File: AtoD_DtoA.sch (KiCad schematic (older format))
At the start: 21 parts

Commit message: redo annotations
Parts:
- gave numbers to parts that had none: 21

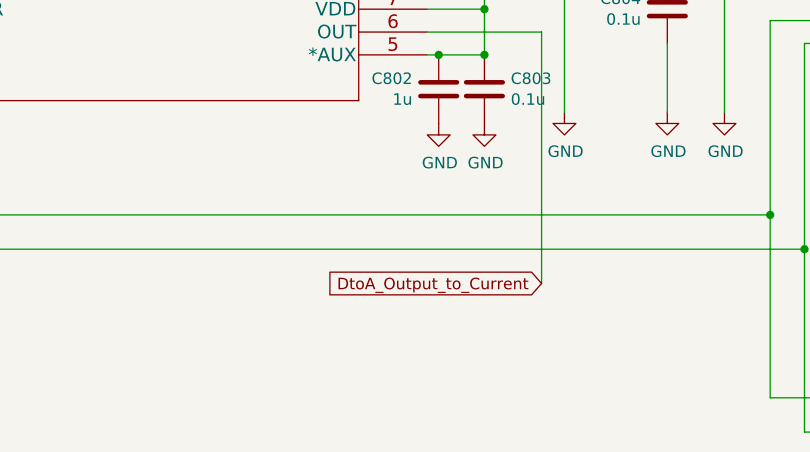
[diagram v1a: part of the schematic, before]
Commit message: made butterfly a global label, connected SDA & SCL
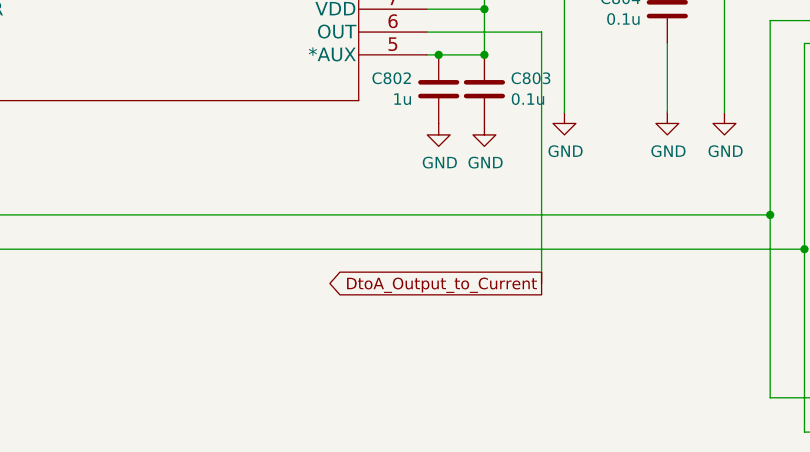
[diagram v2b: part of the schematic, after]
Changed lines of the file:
@@
 Wire Wire Line
 	6900 4550 6900 5650
-Text GLabel 6900 5650 0    50   Input ~ 0
+Text GLabel 6900 5650 0    50   Output ~ 0
 DtoA_Output_to_Current
 Wire Wire Line

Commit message: finish monitor on butterfly
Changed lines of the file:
@@
 	11450 4900 11450 4800
 Wire Wire Line
-	11850 4800 11450 4800
+	11850 4800 11700 4800
 Connection ~ 11450 4800
 Wire Wire Line
@@
 Wire Wire Line
 	10850 3650 10850 4400
+Wire Wire Line
+	11700 4800 11700 5250
+Wire Wire Line
+	11700 5250 11800 5250
+Connection ~ 11700 4800
+Wire Wire Line
+	11700 4800 11450 4800
+Text GLabel 11800 5250 2    50   Input ~ 0
+Monitor+_To_AIN2
 $EndSCHEMATC

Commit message: GND works
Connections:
- net GND: no longer IC801.7 (AIN2)
- new net Monitor+_To_AIN2: IC801.7 (AIN2)
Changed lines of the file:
@@
 Connection ~ 11450 4900
 Wire Wire Line
-	11450 4900 11450 4800
-Wire Wire Line
 	11850 4800 11700 4800
-Connection ~ 11450 4800
-Wire Wire Line
-	11450 4800 11450 4600
 Wire Wire Line
 	11850 4600 11700 4600
@@
 Wire Wire Line
 	11700 5250 11800 5250
-Connection ~ 11700 4800
-Wire Wire Line
-	11700 4800 11450 4800
 Text GLabel 11800 5250 2    50   Input ~ 0
 Monitor+_To_AIN2
+Wire Wire Line
+	11450 4600 11450 4900
 $EndSCHEMATC

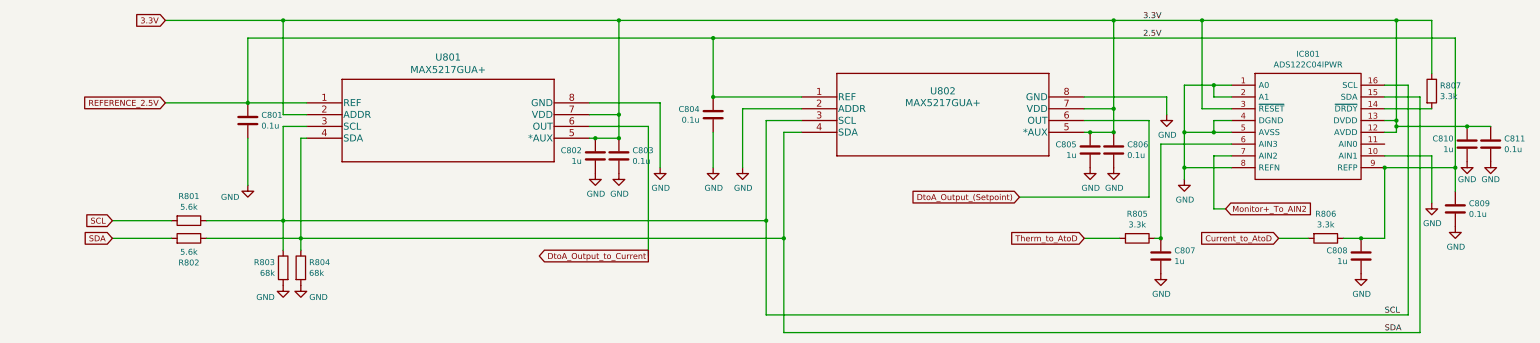
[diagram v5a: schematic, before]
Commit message: finished everything. notes: thick traces, gnd pours, keep outs/pwr plane, DRC Errors
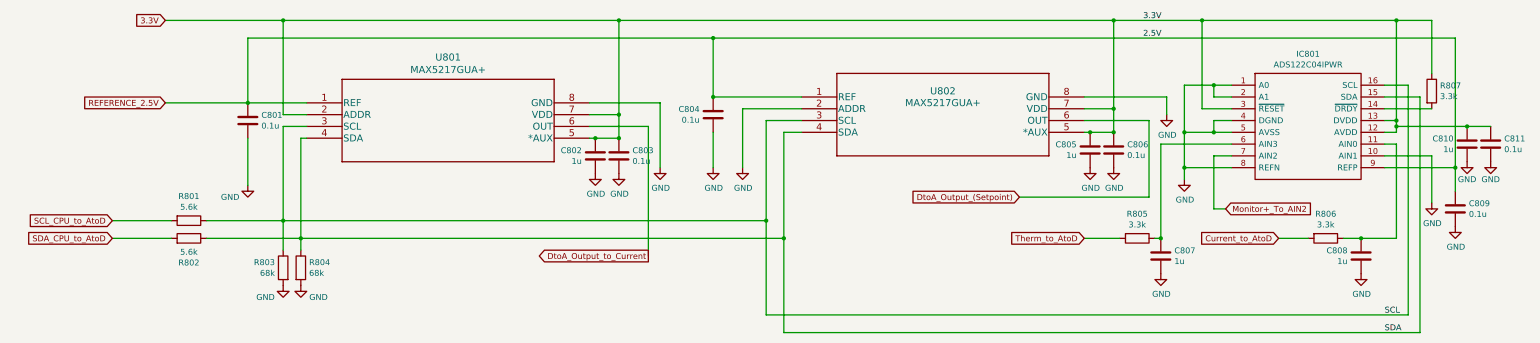
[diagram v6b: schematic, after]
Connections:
- net REFERENCE_2.5V: no longer C808.1, R806.1
- net SCL: no longer R801.2
- net SDA: no longer R802.2
- net at IC801.11 (AIN0): now also C808.1, R806.1
- new net SCL_CPU_to_AtoD: R801.2
- new net SDA_CPU_to_AtoD: R802.2
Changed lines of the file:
@@
 	8200 4600 8050 4600
-Wire Wire Line
-	12950 5500 13150 5500
 Wire Wire Line
 	13350 4200 13350 6150
@@
 DtoA_Output_to_Current
 Wire Wire Line
-	13150 4900 13150 5500
-Connection ~ 13150 4900
-Wire Wire Line
 	7450 3800 3500 3800
 Wire Wire Line
@@
 	2850 5500 2350 5500
 Text GLabel 2350 5350 0    50   Input ~ 0
-SCL
+SCL_CPU_to_AtoD
 Text GLabel 2350 5500 0    50   Input ~ 0
-SDA
+SDA_CPU_to_AtoD
 Text Label 11100 3650 0    50   ~ 0
 3.3V
@@
 Wire Wire Line
 	11450 4600 11450 4900
+Wire Wire Line
+	13250 5500 13250 4700
+Wire Wire Line
+	13250 4700 13150 4700
+Wire Wire Line
+	12950 5500 13250 5500
 $EndSCHEMATC
